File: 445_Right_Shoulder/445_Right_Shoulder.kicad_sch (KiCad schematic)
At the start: 2 parts, among them J1 69167-107HLF, U1 LSM6DSMTR

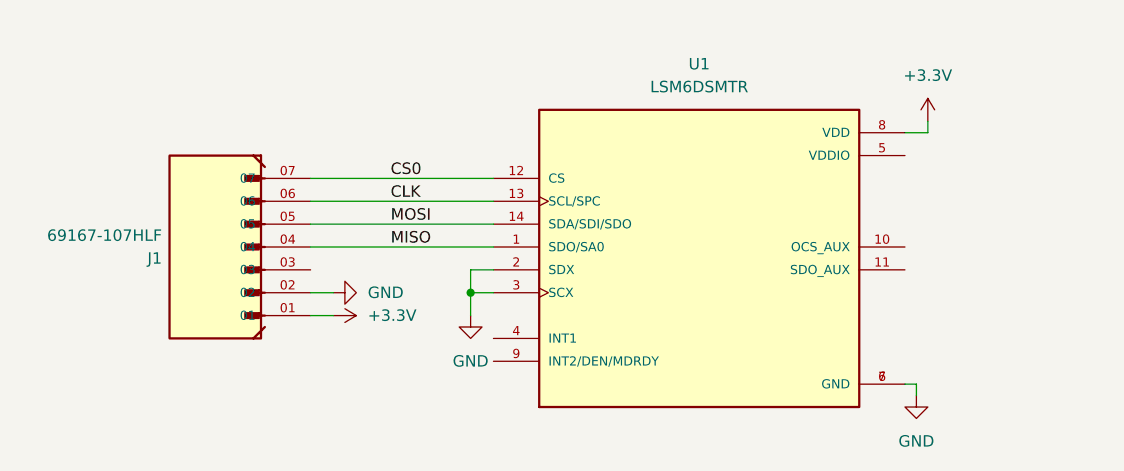
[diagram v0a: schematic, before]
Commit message: enable signal and analog switches
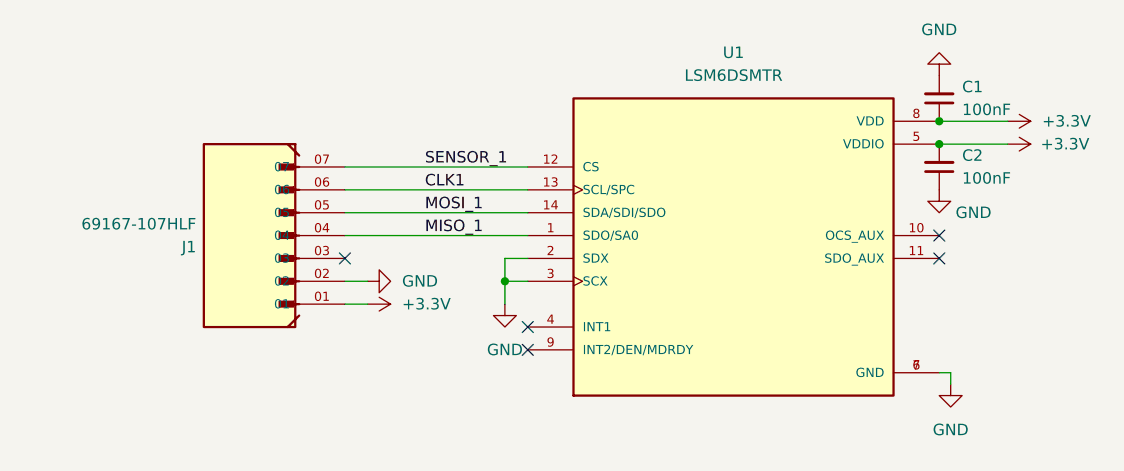
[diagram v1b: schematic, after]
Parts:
- added C1, C2: 100nF, symbol Device:C_Small
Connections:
- net +3.3V: now also U1.5 (VDDIO), C1.1, C2.2
- net GND: now also C1.2, C2.1
- net CLK renamed CLK1
- net CS0 renamed SENSOR_1
- net MISO renamed MISO_1
- net MOSI renamed MOSI_1
- no-connect marks 0 -> 5

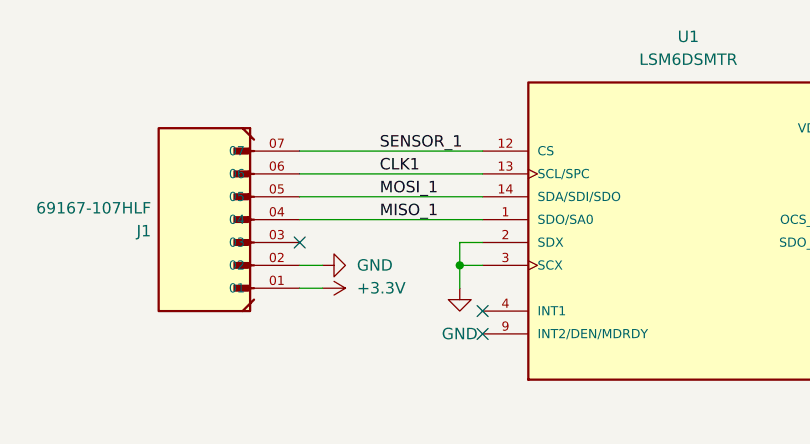
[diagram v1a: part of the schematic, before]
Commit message: replace bicep connector and add int1 connections
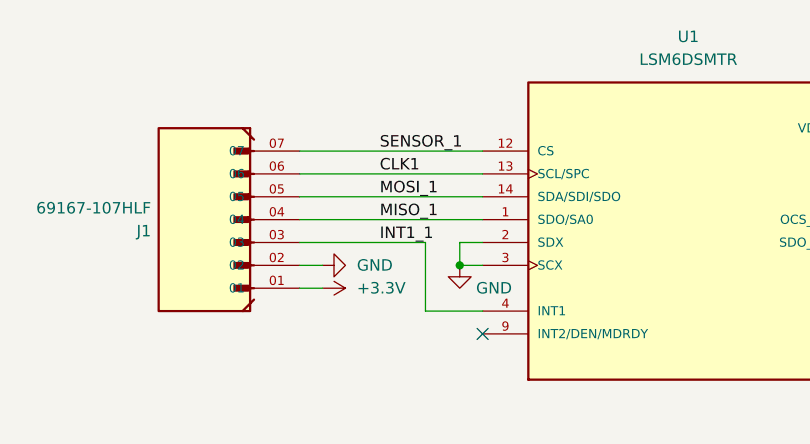
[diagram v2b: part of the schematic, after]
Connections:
- net INT1_1: now reaches U1.4 (INT1)
- net INT1_1: now also J1.03
- no-connect marks 5 -> 3
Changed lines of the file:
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@@
   (junction (at 189.23 76.2) (diameter 0) (color 0 0 0 0)
   )
-  (no_connect (at 143.51 99.06))
-  (no_connect (at 123.19 91.44))
+  (no_connect (at 189.23 91.44))
   (no_connect (at 143.51 101.6))
-  (no_connect (at 189.23 91.44))
   (no_connect (at 189.23 88.9))
-  (wire (pts (xy 140.97 93.98) (xy 140.97 96.52))
-    (stroke (width 0) (type default))
-  )
   (wire (pts (xy 123.19 88.9) (xy 143.51 88.9))
     (stroke (width 0) (type default))
@@
     (stroke (width 0) (type default))
   )
+  (wire (pts (xy 137.16 91.44) (xy 137.16 99.06))
+    (stroke (width 0) (type default))
+  )
   (wire (pts (xy 189.23 104.14) (xy 190.5 104.14))
     (stroke (width 0) (type default))
@@
   )
   (wire (pts (xy 189.23 76.2) (xy 196.85 76.2))
+    (stroke (width 0) (type default))
+  )
+  (wire (pts (xy 123.19 91.44) (xy 137.16 91.44))
+    (stroke (width 0) (type default))
+  )
+  (wire (pts (xy 137.16 99.06) (xy 143.51 99.06))
     (stroke (width 0) (type default))
   )
@@
     (effects (font (size 1.27 1.27)) (justify left bottom))
   )
+  (label "INT1_1" (at 132.08 91.44 0) (fields_autoplaced)
+    (effects (font (size 1.27 1.27)) (justify left bottom))
+  )
   (symbol (lib_id "power:+3.3V") (at 125.73 96.52 270) (unit 1)
     (in_bom yes) (on_board yes) (dnp no) (fields_autoplaced)
@@
     )
   )
-  (symbol (lib_id "power:GND") (at 140.97 96.52 0) (unit 1)
-    (in_bom yes) (on_board yes) (dnp no) (fields_autoplaced)
-    (property "Reference" "#PWR03" (at 140.97 102.87 0)
+  (symbol (lib_id "power:GND") (at 140.97 93.98 0) (unit 1)
+    (in_bom yes) (on_board yes) (dnp no)
+    (property "Reference" "#PWR03" (at 140.97 100.33 0)
       (effects (font (size 1.27 1.27)) hide)
     )
-    (property "Value" "GND" (at 140.97 101.6 0)
+    (property "Value" "GND" (at 144.78 96.52 0)
       (effects (font (size 1.27 1.27)))
     )
-    (property "Footprint" "" (at 140.97 96.52 0)
+    (property "Footprint" "" (at 140.97 93.98 0)
       (effects (font (size 1.27 1.27)) hide)
     )
-    (property "Datasheet" "" (at 140.97 96.52 0)
+    (property "Datasheet" "" (at 140.97 93.98 0)
       (effects (font (size 1.27 1.27)) hide)
     )

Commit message: Layout First Draft
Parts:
- added H1, H2, H3, H4: MountingHole, MountingHole:MountingHole_2mm, symbol Mechanical:MountingHole
- C1, C2: footprint (none) -> CL21F104ZAANNNC:CAPC2012X135N
- renumbered J1 to J3, U1 to U6
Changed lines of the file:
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@@
     (effects (font (size 1.27 1.27)) (justify left bottom))
+  )
+  (symbol (lib_id "Mechanical:MountingHole") (at 24.13 34.29 0) (unit 1)
+    (in_bom yes) (on_board yes) (dnp no) (fields_autoplaced)
+    (property "Reference" "H2" (at 26.67 33.02 0)
+      (effects (font (size 1.27 1.27)) (justify left))
+    )
+    (property "Value" "MountingHole" (at 26.67 35.56 0)
+      (effects (font (size 1.27 1.27)) (justify left))
+    )
+    (property "Footprint" "MountingHole:MountingHole_2mm" (at 24.13 34.29 0)
+      (effects (font (size 1.27 1.27)) hide)
+    )
+    (property "Datasheet" "~" (at 24.13 34.29 0)
+      (effects (font (size 1.27 1.27)) hide)
+    )
+    (instances
+      (project "445_Right_Shoulder"
+        (path "/e6895ae2-6c89-4234-b1b5-3b93ecd658ff"
+          (reference "H2") (unit 1)
+        )
+      )
+    )
   )
   (symbol (lib_id "power:+3.3V") (at 125.73 96.52 270) (unit 1)
@@
     )
   )
+  (symbol (lib_id "Mechanical:MountingHole") (at 24.13 27.94 0) (unit 1)
+    (in_bom yes) (on_board yes) (dnp no) (fields_autoplaced)
+    (property "Reference" "H1" (at 26.67 26.67 0)
+      (effects (font (size 1.27 1.27)) (justify left))
+    )
+    (property "Value" "MountingHole" (at 26.67 29.21 0)
+      (effects (font (size 1.27 1.27)) (justify left))
+    )
+    (property "Footprint" "MountingHole:MountingHole_2mm" (at 24.13 27.94 0)
+      (effects (font (size 1.27 1.27)) hide)
+    )
+    (property "Datasheet" "~" (at 24.13 27.94 0)
+      (effects (font (size 1.27 1.27)) hide)
+    )
+    (instances
+      (project "445_Right_Shoulder"
+        (path "/e6895ae2-6c89-4234-b1b5-3b93ecd658ff"
+          (reference "H1") (unit 1)
+        )
+      )
+    )
+  )
   (symbol (lib_id "power:GND") (at 189.23 71.12 180) (unit 1)
     (in_bom yes) (on_board yes) (dnp no) (fields_autoplaced)
@@
     )
   )
+  (symbol (lib_id "Mechanical:MountingHole") (at 24.13 49.53 0) (unit 1)
+    (in_bom yes) (on_board yes) (dnp no) (fields_autoplaced)
+    (property "Reference" "H4" (at 26.67 48.26 0)
+      (effects (font (size 1.27 1.27)) (justify left))
+    )
+    (property "Value" "MountingHole" (at 26.67 50.8 0)
+      (effects (font (size 1.27 1.27)) (justify left))
+    )
+    (property "Footprint" "MountingHole:MountingHole_2mm" (at 24.13 49.53 0)
+      (effects (font (size 1.27 1.27)) hide)
+    )
+    (property "Datasheet" "~" (at 24.13 49.53 0)
+      (effects (font (size 1.27 1.27)) hide)
+    )
+    (instances
+      (project "445_Right_Shoulder"
+        (path "/e6895ae2-6c89-4234-b1b5-3b93ecd658ff"
+          (reference "H4") (unit 1)
+        )
+      )
+    )
+  )
   (symbol (lib_id "LSM6DSMTR:LSM6DSMTR") (at 166.37 88.9 0) (unit 1)
     (in_bom yes) (on_board yes) (dnp no) (fields_autoplaced)
-    (property "Reference" "U1" (at 166.37 68.58 0)
+    (property "Reference" "U6" (at 166.37 68.58 0)
       (effects (font (size 1.27 1.27)))
     )
@@
       (project "445_Right_Shoulder"
         (path "/e6895ae2-6c89-4234-b1b5-3b93ecd658ff"
-          (reference "U1") (unit 1)
+          (reference "U6") (unit 1)
         )
       )
@@
   (symbol (lib_id "69167-107HLF:69167-107HLF") (at 113.03 88.9 180) (unit 1)
     (in_bom yes) (on_board yes) (dnp no)
-    (property "Reference" "J1" (at 106.68 90.17 0)
+    (property "Reference" "J3" (at 106.68 90.17 0)
       (effects (font (size 1.27 1.27)) (justify left))
     )
@@
       (project "445_Right_Shoulder"
         (path "/e6895ae2-6c89-4234-b1b5-3b93ecd658ff"
-          (reference "J1") (unit 1)
+          (reference "J3") (unit 1)
         )
       )
@@
       (effects (font (size 1.27 1.27)) (justify right))
     )
-    (property "Footprint" "" (at 189.23 73.66 0)
+    (property "Footprint" "CL21F104ZAANNNC:CAPC2012X135N" (at 189.23 73.66 0)
       (effects (font (size 1.27 1.27)) hide)
     )
@@
         (path "/e6895ae2-6c89-4234-b1b5-3b93ecd658ff"
           (reference "C1") (unit 1)
+        )
+      )
+    )
+  )
+  (symbol (lib_id "Mechanical:MountingHole") (at 24.13 41.91 0) (unit 1)
+    (in_bom yes) (on_board yes) (dnp no) (fields_autoplaced)
+    (property "Reference" "H3" (at 26.67 40.64 0)
+      (effects (font (size 1.27 1.27)) (justify left))
+    )
+    (property "Value" "MountingHole" (at 26.67 43.18 0)
+      (effects (font (size 1.27 1.27)) (justify left))
+    )
+    (property "Footprint" "MountingHole:MountingHole_2mm" (at 24.13 41.91 0)
+      (effects (font (size 1.27 1.27)) hide)
+    )
+    (property "Datasheet" "~" (at 24.13 41.91 0)
+      (effects (font (size 1.27 1.27)) hide)
+    )
+    (instances
+      (project "445_Right_Shoulder"
+        (path "/e6895ae2-6c89-4234-b1b5-3b93ecd658ff"
+          (reference "H3") (unit 1)
         )
       )
@@
       (effects (font (size 1.27 1.27)) (justify right))
     )
-    (property "Footprint" "" (at 189.23 81.28 0)
-      (effects (font (size 1.27 1.27)) hide)
-    )
+    (property "Footprint" "CL21F104ZAANNNC:CAPC2012X135N" (at 189.23 81.28 0)
+      (effects (font (size 1.27 1.27)) hide)
+    )
